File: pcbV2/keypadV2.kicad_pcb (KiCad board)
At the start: 2 copper layers, 93.7 x 93.3 mm, 59 parts, among them J1 Conn_01x02_Female, J2 USB_C_Receptacle, J3 Conn_01x03_Male, J6 Conn_01x03_Male, Q1 Q_NMOS_GSD, Q2 Q_NMOS_GSD, SW1 SW_Push, SW10 SW_Push, SW11 SW_Push, SW12 SW_Push, SW13 SW_SPDT, SW14 SW_Push, SW15 SW_Push, SW16 SW_Push, SW17 SW_DIP_x03, SW2 SW_Push, SW3 SW_Push, SW4 SW_Push, SW5 SW_Push, SW6 SW_Push, SW7 SW_Push, SW8 SW_Push, SW9 SW_Push, U1 Teensy4.0, U2 Waveshare_OLED_RGB

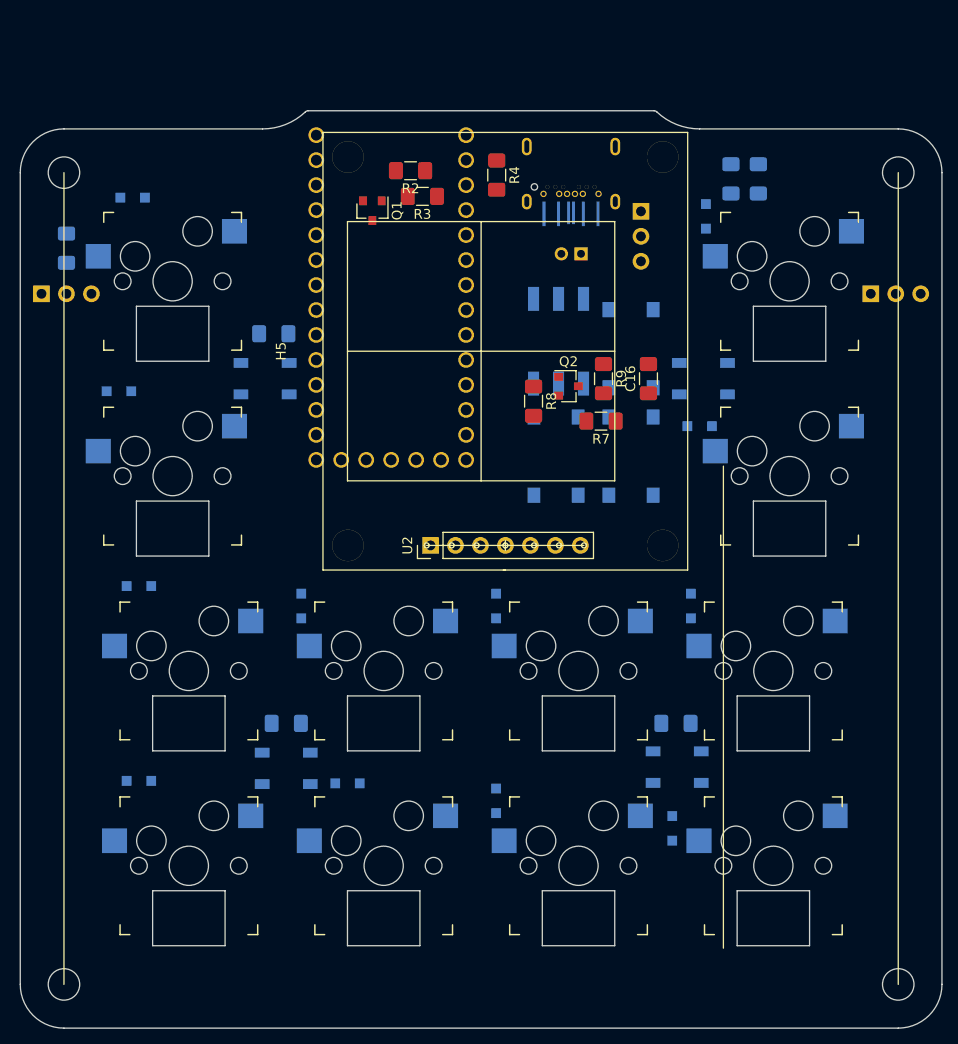
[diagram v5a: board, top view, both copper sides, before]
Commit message: Started laying traces
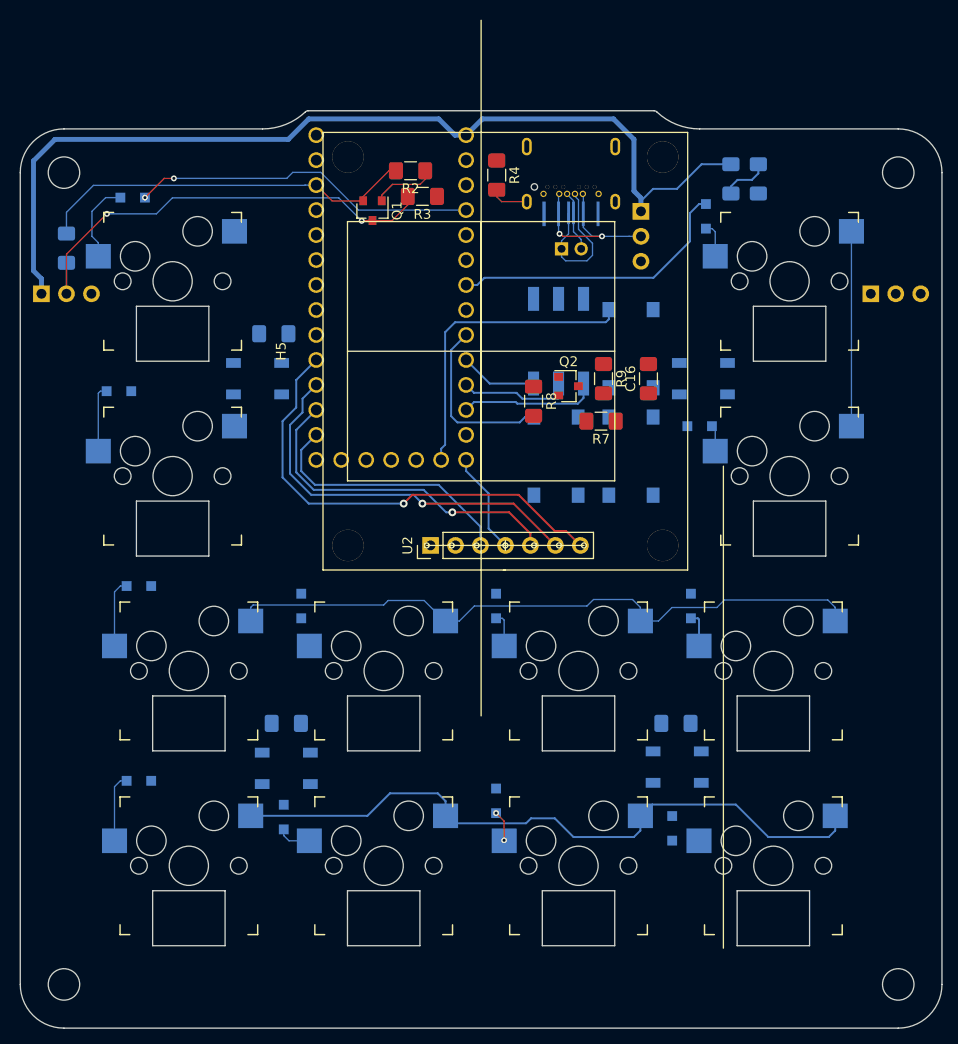
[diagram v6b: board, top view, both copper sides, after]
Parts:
- moved D10 7.33 mm to (101.1, 172.3), turned to 270 degrees
- moved J1 2.05 mm to (129.3, 114.6), turned to 270 degrees
- moved D26 0.76 mm to (98.4, 127.8)
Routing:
- net +5V: track 0.00 -> 98.3 mm
- net ROW3: track 0.00 -> 68.9 mm
- net ROW2: track 0.00 -> 67.2 mm
- net DISP_RST: track 0.00 -> 47.3 mm, vias 0 -> 1
- net RGB_DIN: track 0.00 -> 46.8 mm, vias 0 -> 2
- net DISP_DC: track 0.00 -> 40.1 mm, vias 0 -> 1
- net RGB_DATA1: track 0.00 -> 39.0 mm
- net COL1: track 0.00 -> 35.3 mm, vias 0 -> 2
- net CS: track 0.00 -> 34.8 mm, vias 0 -> 1
- net ON_OFF: track 0.00 -> 31.3 mm
- net COL4: track 0.00 -> 29.5 mm
- net MOSI: track 0.00 -> 26.8 mm
- net ROW1: track 0.00 -> 19.8 mm
- net USB_VBUS: track 0.00 -> 18.2 mm, vias 0 -> 2
- net BTN: track 0.00 -> 17.8 mm
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
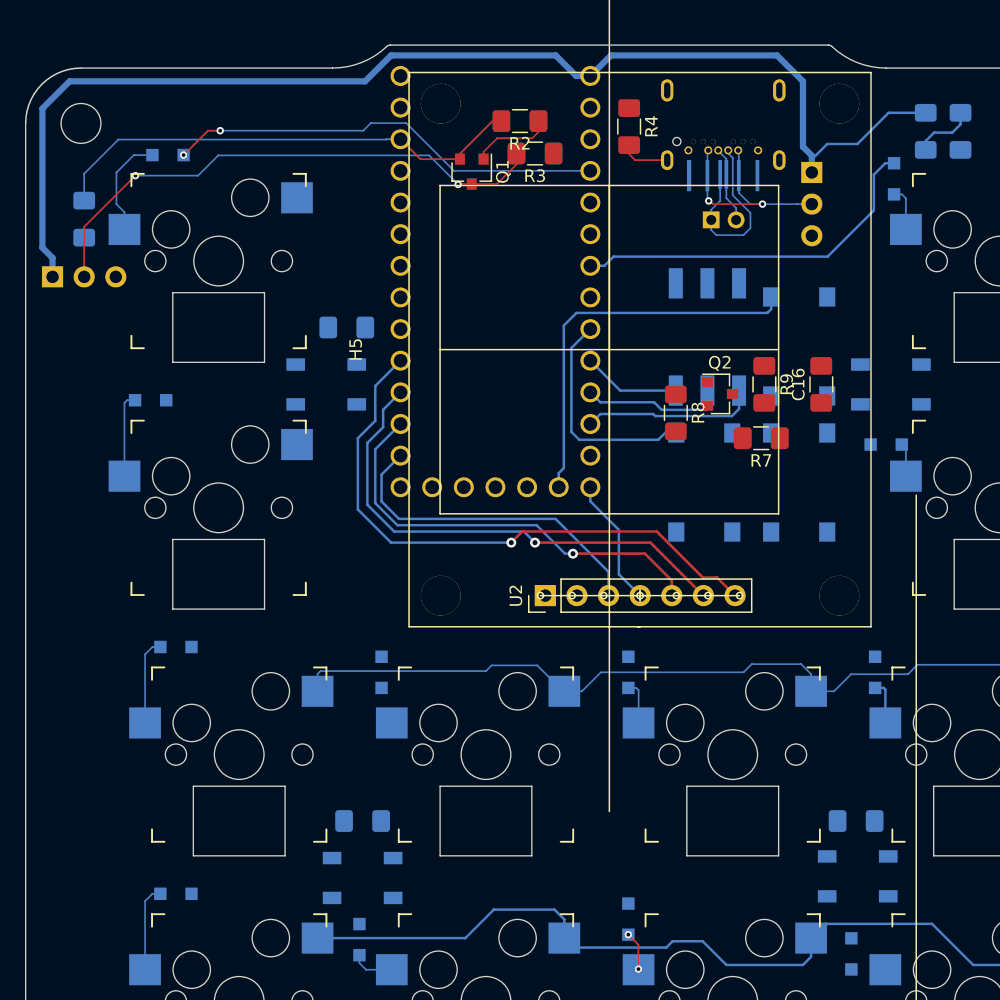
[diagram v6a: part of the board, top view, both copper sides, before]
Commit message: 3.3V was on wrong pin on teens
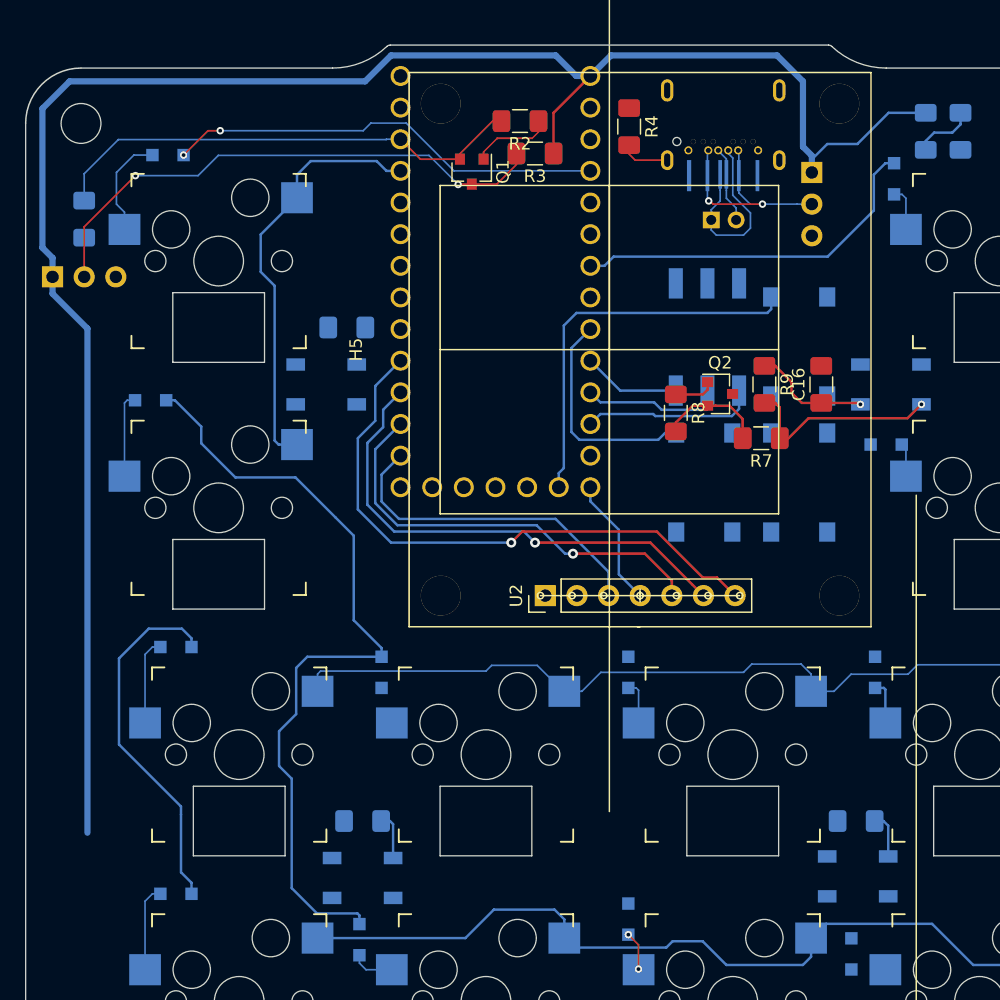
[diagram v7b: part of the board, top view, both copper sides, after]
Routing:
- net +5V: track 98.3 -> 168.5 mm, vias 0 -> 1
- net COL2: track 0.00 -> 63.9 mm
- net ROW1: track 19.8 -> 53.9 mm
- net COL1: track 35.3 -> 64.5 mm
- net RGB_UNDER: track 0.00 -> 16.4 mm, vias 0 -> 1
- net RGB_DATA2: track 0.00 -> 8.63 mm
- net +3V3: track 6.54 -> 9.85 mm

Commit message: finished tracing
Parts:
- moved C13 2.07 mm to (98.0, 122.8)
- moved D26 0.88 mm to (98.1, 126.9)
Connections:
- U1 pad 16: Net-(U1-Pad16) -> +3V3
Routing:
- net +5V: track 168.5 -> 305.6 mm, vias 1 -> 6
- net COL3: track 0.00 -> 102.2 mm, vias 0 -> 5
- net COL4: track 29.5 -> 91.9 mm, vias 0 -> 4
- net ROW1: track 53.9 -> 116.0 mm, vias 0 -> 2
- net ROW3: track 68.9 -> 128.2 mm, vias 0 -> 1
- net +3V3: track 9.85 -> 67.6 mm, vias 0 -> 2
- net Net-(D26-Pad4): track 0.00 -> 55.2 mm, vias 0 -> 6
- net Net-(D27-Pad4): track 0.00 -> 51.7 mm
- net COL1: track 64.5 -> 111.7 mm
- net Net-(D28-Pad4): track 0.00 -> 44.5 mm, vias 0 -> 2
- net COL2: track 63.9 -> 106.0 mm, vias 0 -> 2
- net ROW2: track 67.2 -> 109.2 mm, vias 0 -> 1
- net PRGM: track 0.00 -> 25.6 mm, vias 0 -> 1
- net ON_OFF: track 31.3 -> 48.6 mm, vias 0 -> 2
- net RGB_DATA2: track 8.63 -> 17.3 mm, vias 0 -> 1
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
